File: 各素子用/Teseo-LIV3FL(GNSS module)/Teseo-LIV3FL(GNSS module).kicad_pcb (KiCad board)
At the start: 2 copper layers, 20 x 27.5 mm, 8 parts, among them IC1 TESEO-LIV3FL, J1 Conn_Coaxial, J2 Conn_01x05_Pin

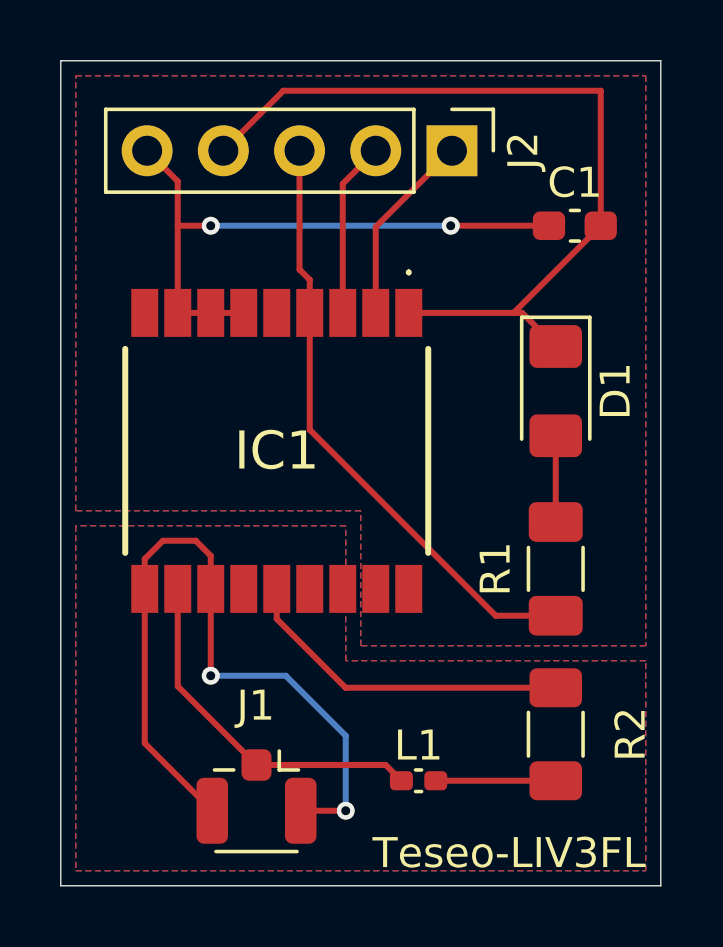
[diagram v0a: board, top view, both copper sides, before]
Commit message: Change board width
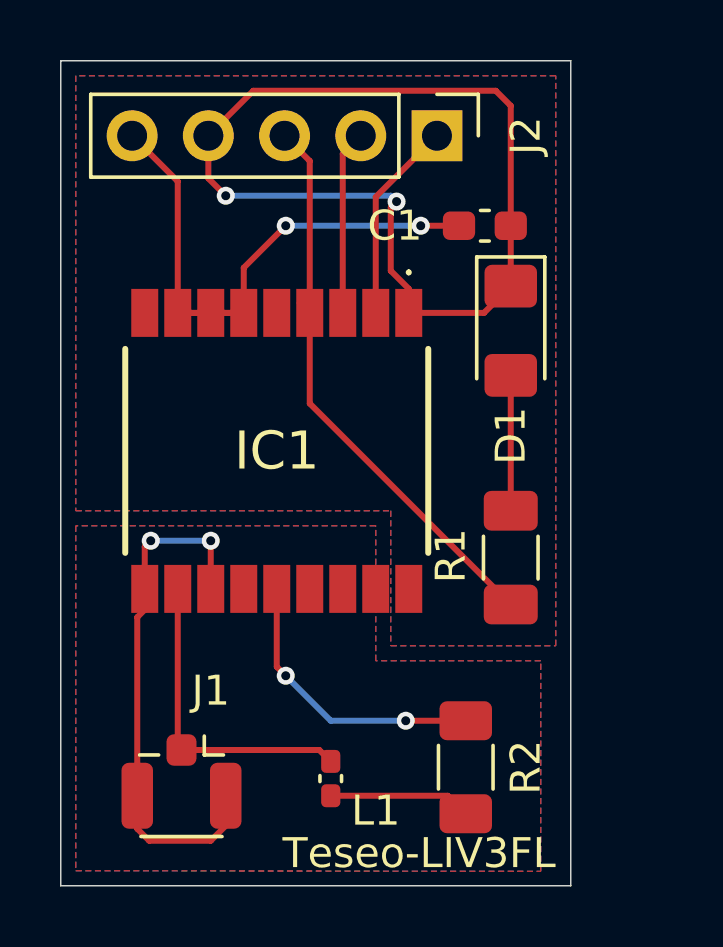
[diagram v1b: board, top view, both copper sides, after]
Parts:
- moved R2 3.20 mm to (83.5, 73.5)
- moved C1 3.00 mm to (84.1, 55.5)
- moved L1 2.93 mm to (79.0, 73.9), turned to -90 degrees
- moved J1 2.55 mm to (74.0, 74.0)
- moved D1 2.51 mm to (85.0, 59.0)
- moved R1 1.55 mm to (85.0, 66.6)
- moved J2 0.71 mm to (82.5, 52.5)
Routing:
- net GND1: track 25.3 -> 17.7 mm
- net GND: track 27.4 -> 32.7 mm, vias 0 -> 2
- net Net-(D1-A): track 2.88 -> 4.51 mm
- net Net-(IC1-VCC_RF): track 11.3 -> 9.64 mm, vias 0 -> 2
- net Net-(IC1-1PPS): track 20.7 -> 19.2 mm
- net Net-(IC1-RF_IN): track 12.0 -> 10.6 mm
- net Net-(L1-Pad2): track 4.00 -> 4.75 mm
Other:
- board size 20 x 27.5 mm -> 17 x 27.5 mm
